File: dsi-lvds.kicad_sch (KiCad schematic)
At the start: 22 parts, among them U1 TLV70018_SC70, U16 SN65DSI84, U2 TXB0104_UQFN

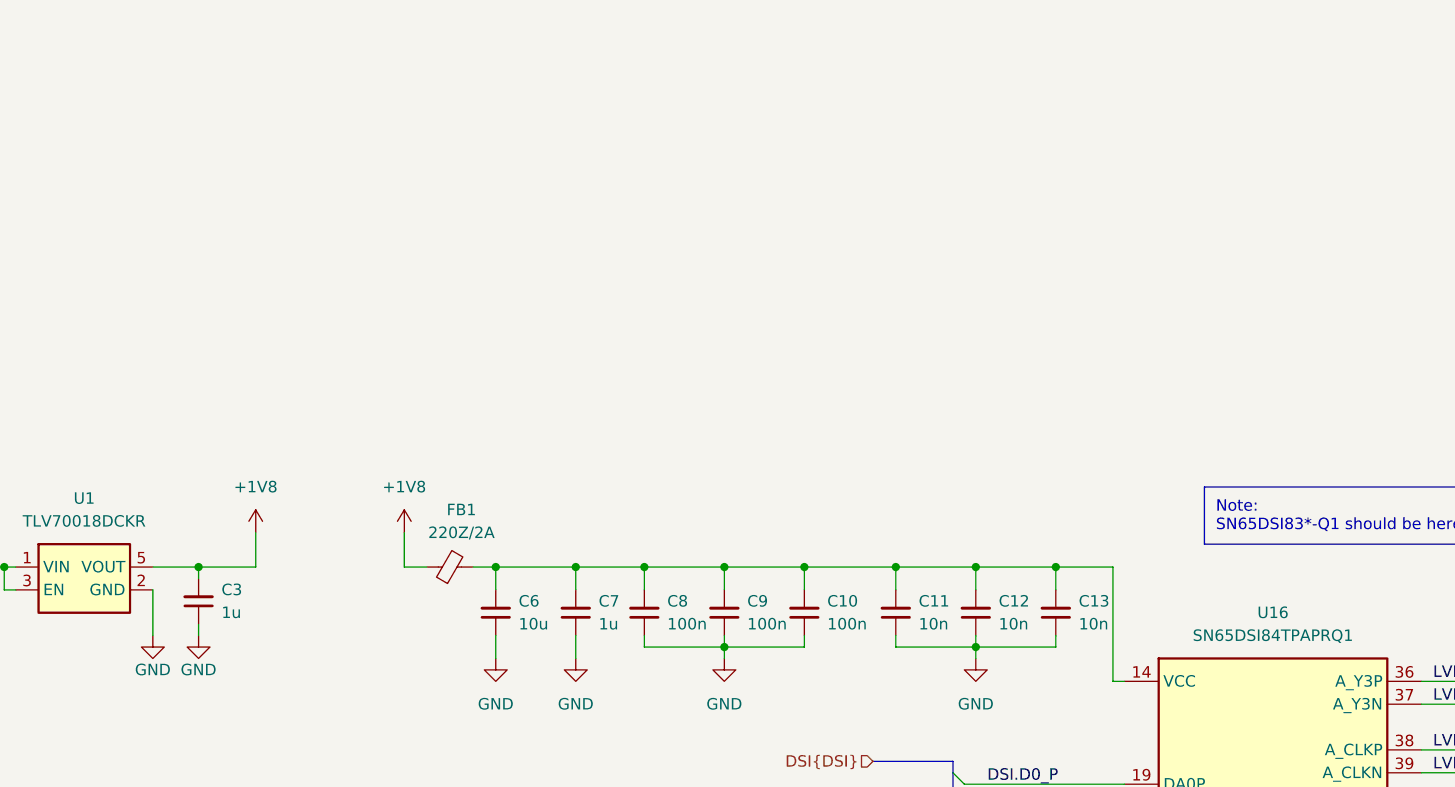
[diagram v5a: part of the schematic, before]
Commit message: [#54932] Add power indicators
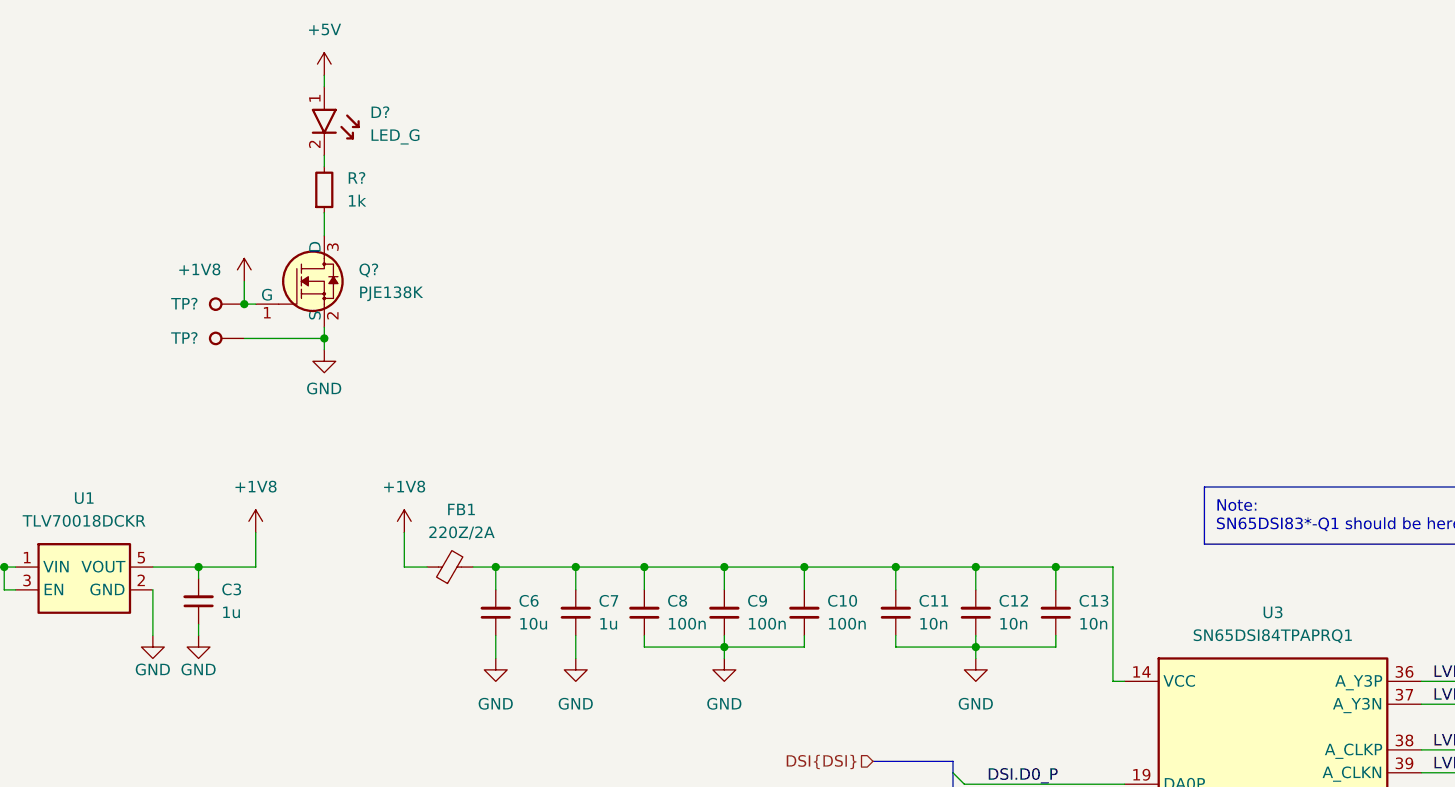
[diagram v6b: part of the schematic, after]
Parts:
- added D?: LED_G, antmicro-footprints:LED_0603_1608Metric_R, symbol antmicroLEDIndicationDiscrete:LED_R_0603_598-8D80-107F
- added Q?: PJE138K, antmicro-footprints:SOT-523, symbol antmicroTransistorsFETsMOSFETsSingle:PJE138K
- added R?: R_1k_0402, antmicro-footprints:R_0402_1005Metric, symbol antmicroResistors0402:R_1k_0402
- added TP? (x2): TP_1mm_SMD, antmicro-footprints:TP_SMD_1mm, symbol antmicroTestPoints:TP_1mm_SMD
- renumbered U16 to U3
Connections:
- net +1V8: now also Q?.1 (G), TP?.1
- net GND: now also Q?.2 (S), TP?.1
- new net: Q?.3 (D), R?.1
- new net: D?.2, R?.2
- new net +5V: D?.1

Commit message: [#54932] Reanotate schematics
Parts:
- gave numbers to parts that had none: 5
- renumbered R1 to R4, R2 to R5, R3 to R6, R4 to R7, R5 to R8

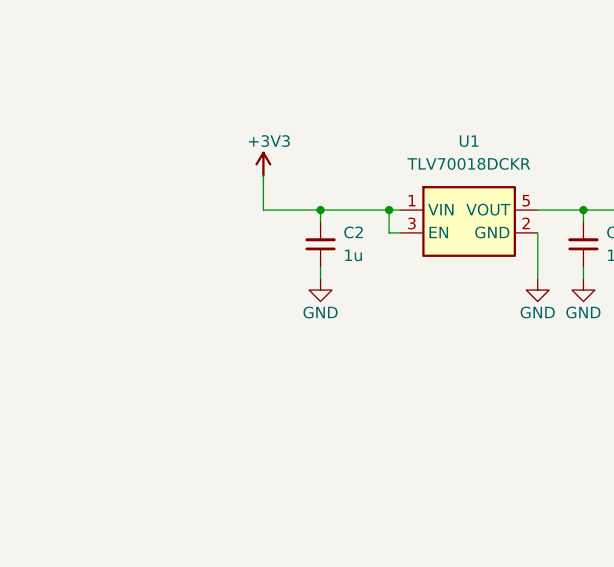
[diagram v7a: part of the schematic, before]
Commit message: [#54932] Connect display to ~{RST}; Connect 1V8 LDO to EN; Fix bus definition
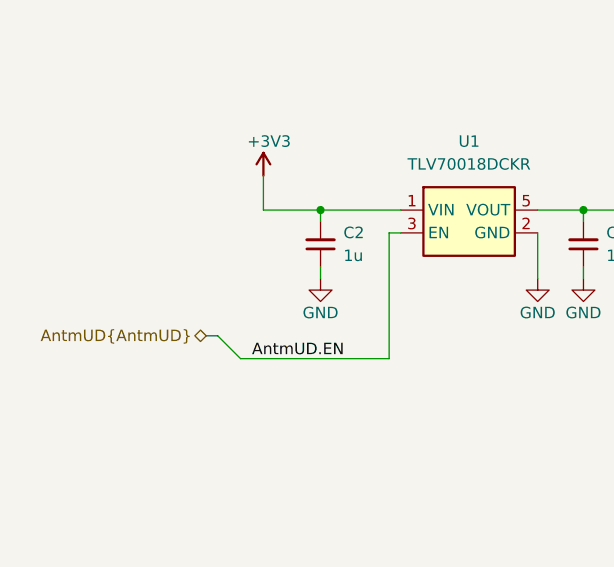
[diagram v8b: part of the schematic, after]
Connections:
- net +3V3: no longer U1.3 (EN)
- net AntmUD.EN: now also U1.3 (EN)
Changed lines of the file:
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@@
   (junction (at 193.04 78.74) (diameter 0) (color 0 0 0 0)
-  )
-  (junction (at 121.92 78.74) (diameter 0) (color 0 0 0 0)
   )
   (junction (at 219.71 137.16) (diameter 0) (color 0 0 0 0)
@@
     (stroke (width 0) (type default))
   )
+  (bus_entry (at 102.87 92.71) (size 2.54 2.54)
+    (stroke (width 0) (type default))
+  )
   (bus_entry (at 227.33 111.76) (size 1.27 1.27)
     (stroke (width 0) (type default))
@@
     (stroke (width 0) (type default))
   )
+  (wire (pts (xy 105.41 95.25) (xy 121.92 95.25))
+    (stroke (width 0) (type default))
+  )
   (wire (pts (xy 229.87 87.63) (xy 238.76 87.63))
     (stroke (width 0) (type default))
@@
     (stroke (width 0) (type default))
   )
-  (wire (pts (xy 114.3 78.74) (xy 121.92 78.74))
+  (wire (pts (xy 114.3 78.74) (xy 123.19 78.74))
     (stroke (width 0) (type default))
   )
@@
     (stroke (width 0) (type default))
   )
-  (wire (pts (xy 121.92 78.74) (xy 123.19 78.74))
-    (stroke (width 0) (type default))
-  )
   (wire (pts (xy 220.98 78.74) (xy 229.87 78.74))
     (stroke (width 0) (type default))
@@
     (stroke (width 0) (type default))
   )
+  (wire (pts (xy 121.92 95.25) (xy 121.92 81.28))
+    (stroke (width 0) (type default))
+  )
   (wire (pts (xy 219.71 137.16) (xy 246.38 137.16))
     (stroke (width 0) (type default))
@@
     (stroke (width 0) (type default))
   )
-  (wire (pts (xy 121.92 81.28) (xy 121.92 78.74))
-    (stroke (width 0) (type default))
-  )
   (bus (pts (xy 227.33 101.6) (xy 227.33 104.14))
     (stroke (width 0) (type default))
@@
     (stroke (width 0) (type default))
   )
-  (wire (pts (xy 123.19 81.28) (xy 121.92 81.28))
+  (wire (pts (xy 121.92 81.28) (xy 123.19 81.28))
     (stroke (width 0) (type default))
   )
@@
   )
   (wire (pts (xy 148.59 53.34) (xy 157.48 53.34))
+    (stroke (width 0) (type default))
+  )
+  (bus (pts (xy 101.6 92.71) (xy 102.87 92.71))
     (stroke (width 0) (type default))
   )
@@
     (effects (font (size 1.27 1.27)) (justify left bottom))
   )
+  (label "AntmUD.EN" (at 106.68 95.25 0) (fields_autoplaced)
+    (effects (font (size 1.27 1.27)) (justify left bottom))
+  )
   (label "LVDS.D3_N" (at 280.67 93.98 0) (fields_autoplaced)
     (effects (font (size 1.27 1.27)) (justify left bottom))
@@
     (effects (font (size 1.27 1.27)) (justify left bottom))
   )
+  (hierarchical_label "AntmUD{AntmUD}" (shape bidirectional) (at 101.6 92.71 180) (fields_autoplaced)
+    (effects (font (size 1.27 1.27)) (justify right))
+  )
   (hierarchical_label "AntmUD{AntmUD}" (shape bidirectional) (at 120.65 200.66 180) (fields_autoplaced)
